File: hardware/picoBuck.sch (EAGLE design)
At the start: 29 parts

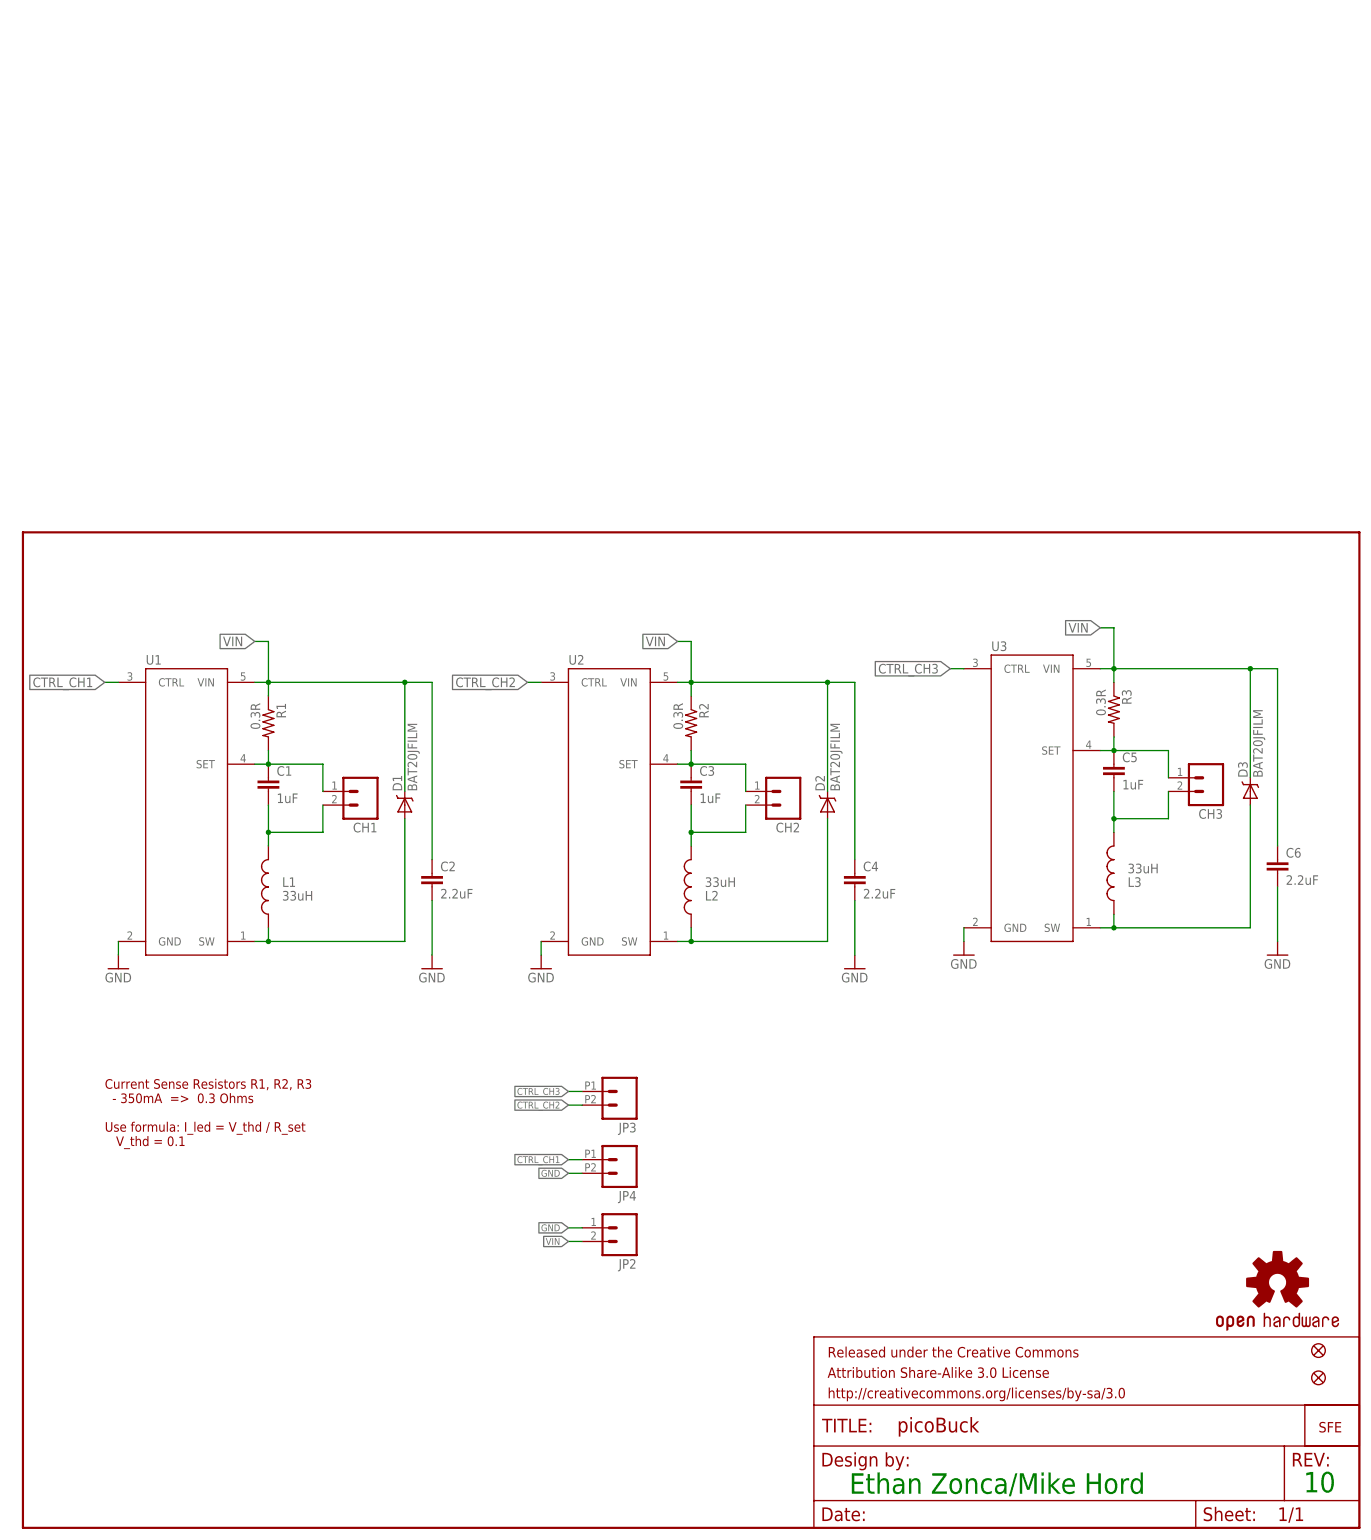
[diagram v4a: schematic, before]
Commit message: High power initial revision - added 2nd sense resistor and solder jumper - changed diode to higher voltage version - changed input cap to higher voltage version
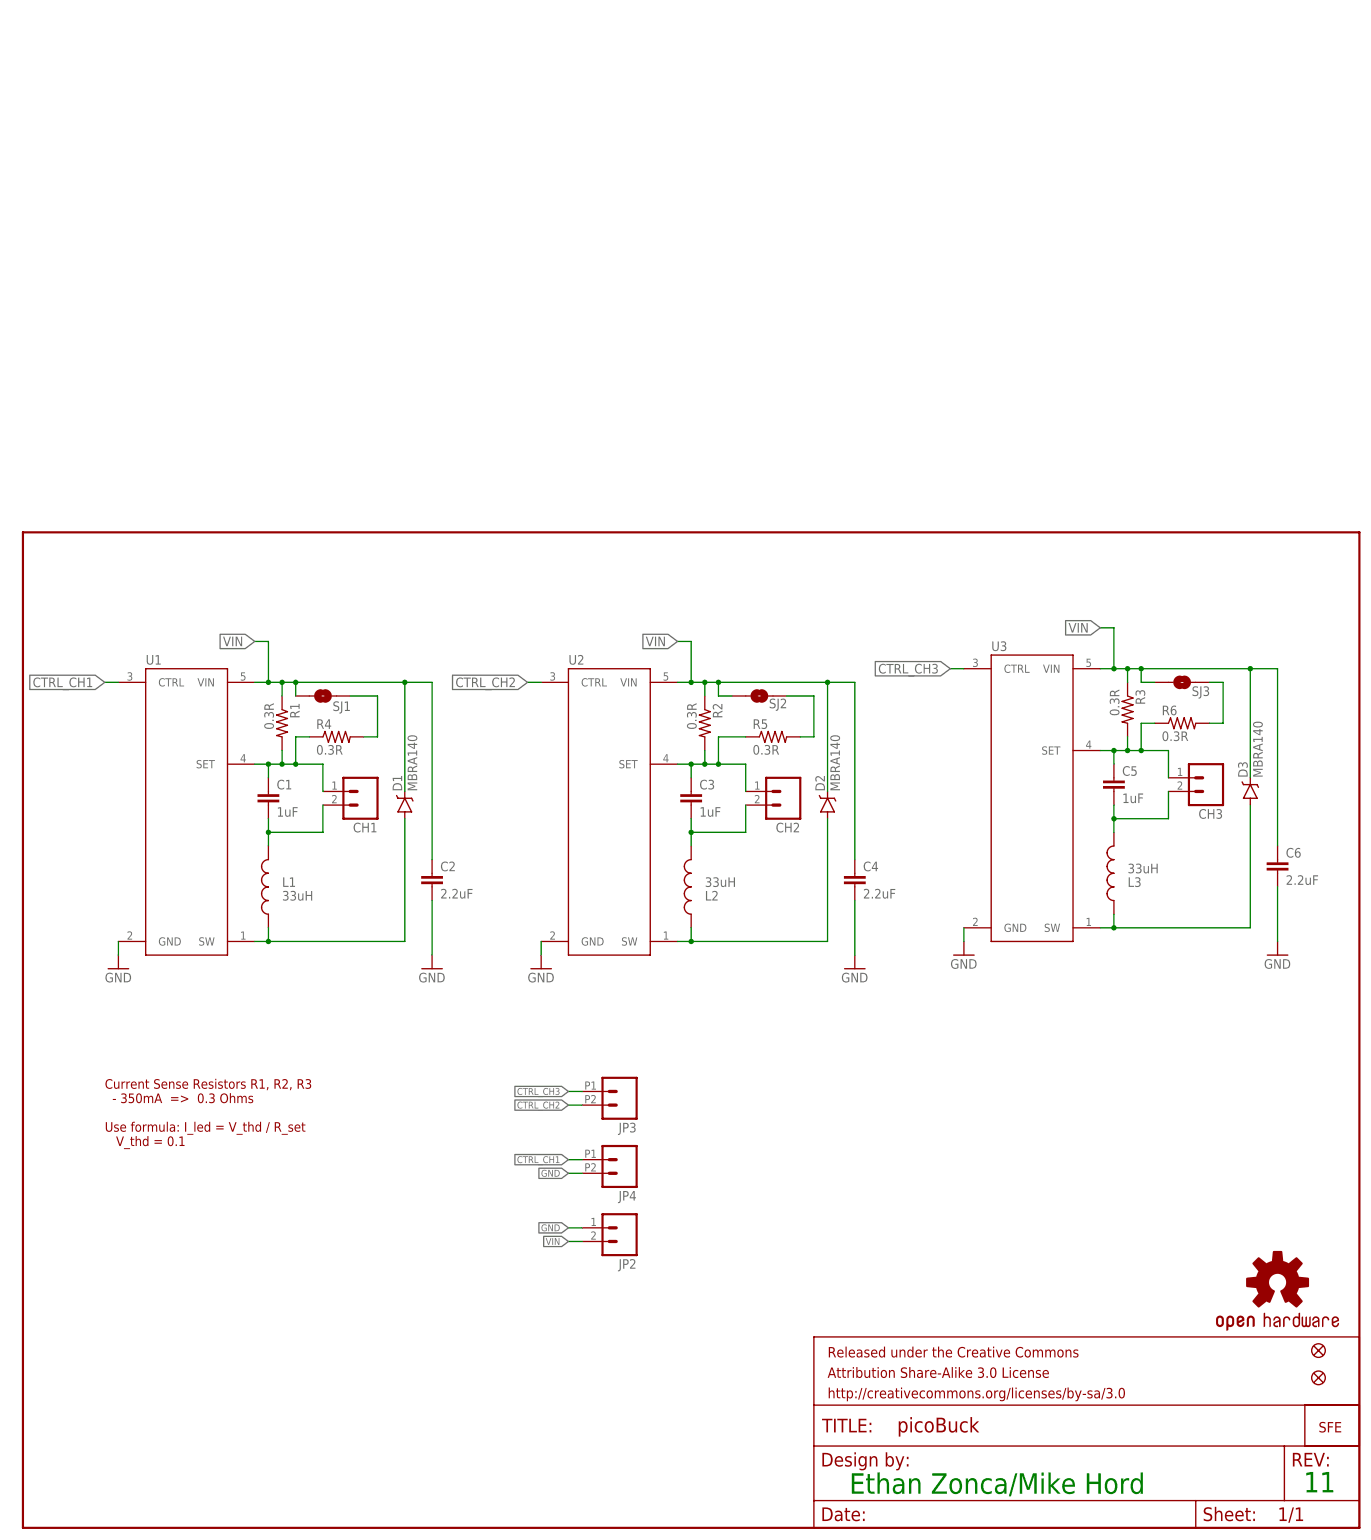
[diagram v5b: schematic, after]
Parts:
- added R4, R5, R6: 0.3R, SparkFun-Resistors:0.3OHM-1/8W-1%(0805)
- added SJ1, SJ2, SJ3: JUMPER-PAD-2-NO, SparkFun-Passives:JUMPER-PAD-2-NO
- D1, D2, D3: value BAT20JFILM -> MBRA140; device SparkFun-DiscreteSemi:BAT20JFILM -> SparkFun-DiscreteSemi:DIODE-SCHOTTKY-MBRA140
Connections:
- removed net N$18: C5.1, CH3.1, R3.2, U3.SET
- new net N$1: C5.1, CH3.1, R3.2, R6.1, U3.SET
- new net N$2: R4.2, SJ1.2
- new net N$3: R5.2, SJ2.2
- new net N$7: R6.2, SJ3.2
- net N$11: now also R4.1
- net N$13: now also R5.1
- net VIN: now also SJ1.1, SJ2.1, SJ3.1
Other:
- note added: "11"
- note removed: "10"
- moved on the sheet: C1, C3, C5, R1, R2, R3

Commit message: Make files as they were before I started monkeying with them
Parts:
- added STANDOFF1, STANDOFF2: STAND-OFF, SparkFun-Electromechanical:STAND-OFF
- U1, U2, U3: value (none) -> AL8805
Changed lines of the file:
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@@
 </classes>
 <parts>
-<part name="U2" library="SparkFun-PowerIC" deviceset="AL8805" device=""/>
+<part name="U2" library="SparkFun-PowerIC" deviceset="AL8805" device="" value="AL8805"/>
 <part name="R2" library="SparkFun-Resistors" deviceset="0.3OHM-1/8W-1%(0805)" device="" value="0.3R"/>
 <part name="C3" library="SparkFun-Capacitors" deviceset="1.0UF-25V-+80/-20(0805)" device="" value="1uF"/>
@@
 <part name="GND12" library="SparkFun" deviceset="GND" device=""/>
 <part name="GND1" library="SparkFun" deviceset="GND" device=""/>
-<part name="U1" library="SparkFun-PowerIC" deviceset="AL8805" device=""/>
+<part name="U1" library="SparkFun-PowerIC" deviceset="AL8805" device="" value="AL8805"/>
 <part name="R1" library="SparkFun-Resistors" deviceset="0.3OHM-1/8W-1%(0805)" device="" value="0.3R"/>
 <part name="C1" library="SparkFun-Capacitors" deviceset="1.0UF-25V-+80/-20(0805)" device="" value="1uF"/>
@@
 <part name="GND6" library="SparkFun" deviceset="GND" device=""/>
 <part name="GND13" library="SparkFun" deviceset="GND" device=""/>
-<part name="U3" library="SparkFun-PowerIC" deviceset="AL8805" device=""/>
+<part name="U3" library="SparkFun-PowerIC" deviceset="AL8805" device="" value="AL8805"/>
 <part name="R3" library="SparkFun-Resistors" deviceset="0.3OHM-1/8W-1%(0805)" device="" value="0.3R"/>
 <part name="C6" library="SparkFun-Capacitors" deviceset="2.2UF-25V-+80/-20(0805)" device="" value="2.2uF"/>
@@
 <part name="R5" library="SparkFun-Resistors" deviceset="0.3OHM-1/8W-1%(0805)" device="" value="0.3R"/>
 <part name="R6" library="SparkFun-Resistors" deviceset="0.3OHM-1/8W-1%(0805)" device="" value="0.3R"/>
+<part name="STANDOFF1" library="SparkFun-Electromechanical" deviceset="STAND-OFF" device=""/>
+<part name="STANDOFF2" library="SparkFun-Electromechanical" deviceset="STAND-OFF" device=""/>
 </parts>
 <sheets>
@@
 <instance part="LOGO2" gate="G$1" x="241.3" y="17.78"/>
 <instance part="FRAME1" gate="G$1" x="0" y="0"/>
-<instance part="FRAME1" gate="G$2" x="147.32" y="0"/>
+<instance part="FRAME1" gate="V" x="147.32" y="0"/>
 <instance part="JP3" gate="G$1" x="111.76" y="81.28" smashed="yes" rot="R180">
 <attribute name="NAME" x="114.3" y="75.438" size="1.778" layer="95" rot="R180"/>
@@
 <instance part="R5" gate="G$1" x="139.7" y="147.32"/>
 <instance part="R6" gate="G$1" x="215.9" y="149.86"/>
+<instance part="STANDOFF1" gate="G$1" x="236.22" y="27.94"/>
+<instance part="STANDOFF2" gate="G$1" x="236.22" y="33.02"/>
 </instances>
 <busses>

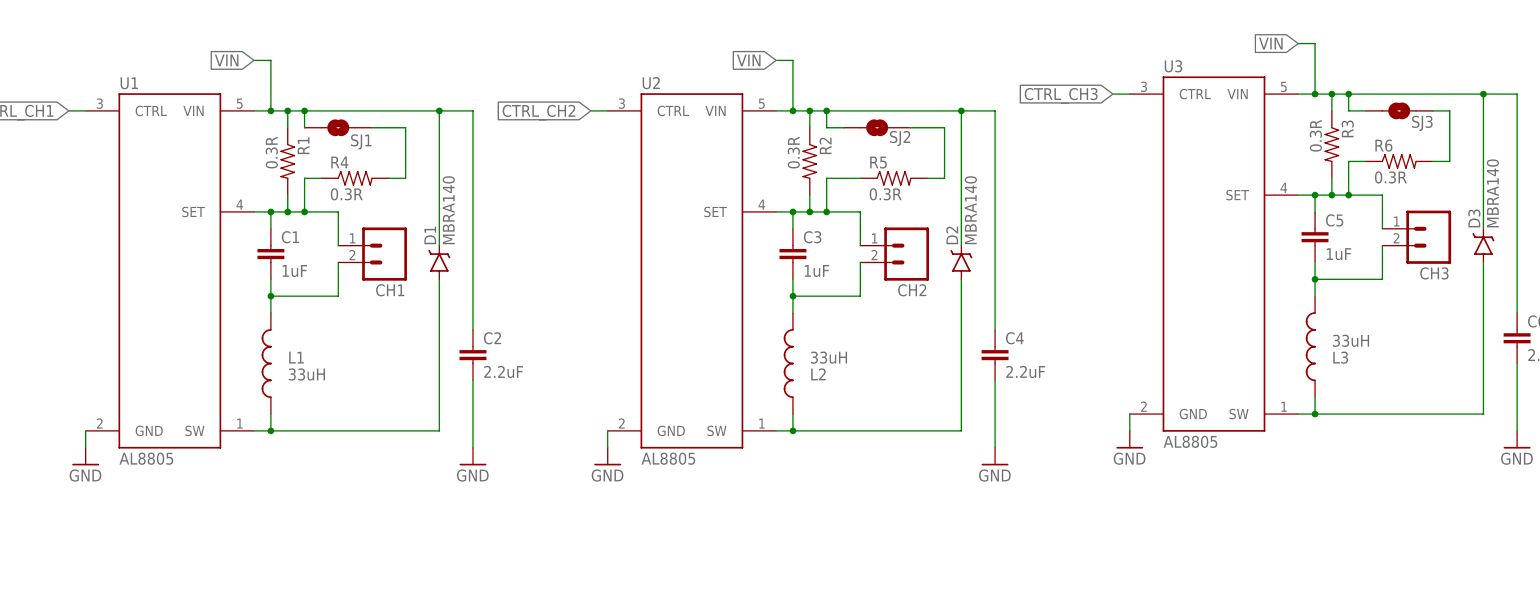
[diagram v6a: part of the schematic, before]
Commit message: Updated library for some silk changes
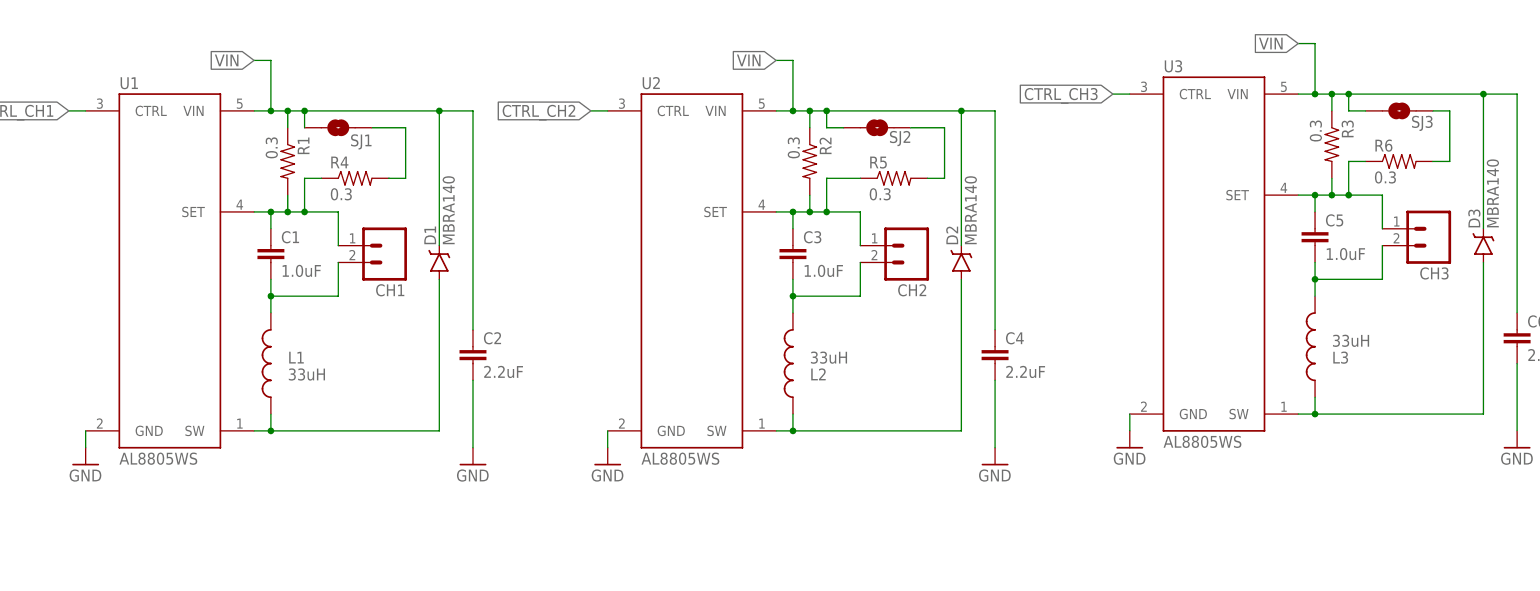
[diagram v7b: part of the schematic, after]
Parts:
- C1, C3, C5: value 1uF -> 1.0uF; device SparkFun-Capacitors:1.0UF-25V-+80/-20(0805) -> SparkFun-Capacitors:1.0UF-25V-+80/-20(0805)"
- R1, R2, R3, R4, R5, R6: value 0.3R -> 0.3
- U1, U2, U3: value AL8805 -> AL8805WS
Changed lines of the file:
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@@
 </classes>
 <parts>
-<part name="U2" library="SparkFun-PowerIC" deviceset="AL8805" device="" value="AL8805"/>
-<part name="R2" library="SparkFun-Resistors" deviceset="0.3OHM-1/8W-1%(0805)" device="" value="0.3R"/>
-<part name="C3" library="SparkFun-Capacitors" deviceset="1.0UF-25V-+80/-20(0805)" device="" value="1uF"/>
+<part name="U2" library="SparkFun-PowerIC" deviceset="AL8805" device="" value="AL8805WS"/>
+<part name="R2" library="SparkFun-Resistors" deviceset="0.3OHM-1/8W-1%(0805)" device="" value="0.3"/>
+<part name="C3" library="SparkFun-Capacitors" deviceset="1.0UF-25V-+80/-20(0805)" device="&quot;" value="1.0uF"/>
 <part name="C4" library="SparkFun-Capacitors" deviceset="2.2UF-25V-+80/-20(0805)" device="" value="2.2uF"/>
 <part name="GND12" library="SparkFun" deviceset="GND" device=""/>
 <part name="GND1" library="SparkFun" deviceset="GND" device=""/>
-<part name="U1" library="SparkFun-PowerIC" deviceset="AL8805" device="" value="AL8805"/>
-<part name="R1" library="SparkFun-Resistors" deviceset="0.3OHM-1/8W-1%(0805)" device="" value="0.3R"/>
-<part name="C1" library="SparkFun-Capacitors" deviceset="1.0UF-25V-+80/-20(0805)" device="" value="1uF"/>
+<part name="U1" library="SparkFun-PowerIC" deviceset="AL8805" device="" value="AL8805WS"/>
+<part name="R1" library="SparkFun-Resistors" deviceset="0.3OHM-1/8W-1%(0805)" device="" value="0.3"/>
+<part name="C1" library="SparkFun-Capacitors" deviceset="1.0UF-25V-+80/-20(0805)" device="&quot;" value="1.0uF"/>
 <part name="C2" library="SparkFun-Capacitors" deviceset="2.2UF-25V-+80/-20(0805)" device="" value="2.2uF"/>
 <part name="GND6" library="SparkFun" deviceset="GND" device=""/>
 <part name="GND13" library="SparkFun" deviceset="GND" device=""/>
-<part name="U3" library="SparkFun-PowerIC" deviceset="AL8805" device="" value="AL8805"/>
-<part name="R3" library="SparkFun-Resistors" deviceset="0.3OHM-1/8W-1%(0805)" device="" value="0.3R"/>
+<part name="U3" library="SparkFun-PowerIC" deviceset="AL8805" device="" value="AL8805WS"/>
+<part name="R3" library="SparkFun-Resistors" deviceset="0.3OHM-1/8W-1%(0805)" device="" value="0.3"/>
 <part name="C6" library="SparkFun-Capacitors" deviceset="2.2UF-25V-+80/-20(0805)" device="" value="2.2uF"/>
 <part name="GND14" library="SparkFun" deviceset="GND" device=""/>
@@
 <part name="CH1" library="SparkFun" deviceset="M02" device="3.5MM_LOCK"/>
 <part name="CH3" library="SparkFun" deviceset="M02" device="3.5MM_LOCK"/>
-<part name="C5" library="SparkFun-Capacitors" deviceset="1.0UF-25V-+80/-20(0805)" device="" value="1uF"/>
+<part name="C5" library="SparkFun-Capacitors" deviceset="1.0UF-25V-+80/-20(0805)" device="&quot;" value="1.0uF"/>
 <part name="D1" library="SparkFun-DiscreteSemi" deviceset="DIODE-SCHOTTKY" device="-MBRA140" value="MBRA140"/>
 <part name="D2" library="SparkFun-DiscreteSemi" deviceset="DIODE-SCHOTTKY" device="-MBRA140" value="MBRA140"/>
@@
 <part name="SJ2" library="SparkFun-Passives" deviceset="JUMPER-PAD-2-NO" device=""/>
 <part name="SJ3" library="SparkFun-Passives" deviceset="JUMPER-PAD-2-NO" device=""/>
-<part name="R4" library="SparkFun-Resistors" deviceset="0.3OHM-1/8W-1%(0805)" device="" value="0.3R"/>
-<part name="R5" library="SparkFun-Resistors" deviceset="0.3OHM-1/8W-1%(0805)" device="" value="0.3R"/>
-<part name="R6" library="SparkFun-Resistors" deviceset="0.3OHM-1/8W-1%(0805)" device="" value="0.3R"/>
+<part name="R4" library="SparkFun-Resistors" deviceset="0.3OHM-1/8W-1%(0805)" device="" value="0.3"/>
+<part name="R5" library="SparkFun-Resistors" deviceset="0.3OHM-1/8W-1%(0805)" device="" value="0.3"/>
+<part name="R6" library="SparkFun-Resistors" deviceset="0.3OHM-1/8W-1%(0805)" device="" value="0.3"/>
 <part name="STANDOFF1" library="SparkFun-Electromechanical" deviceset="STAND-OFF" device=""/>
 <part name="STANDOFF2" library="SparkFun-Electromechanical" deviceset="STAND-OFF" device=""/>

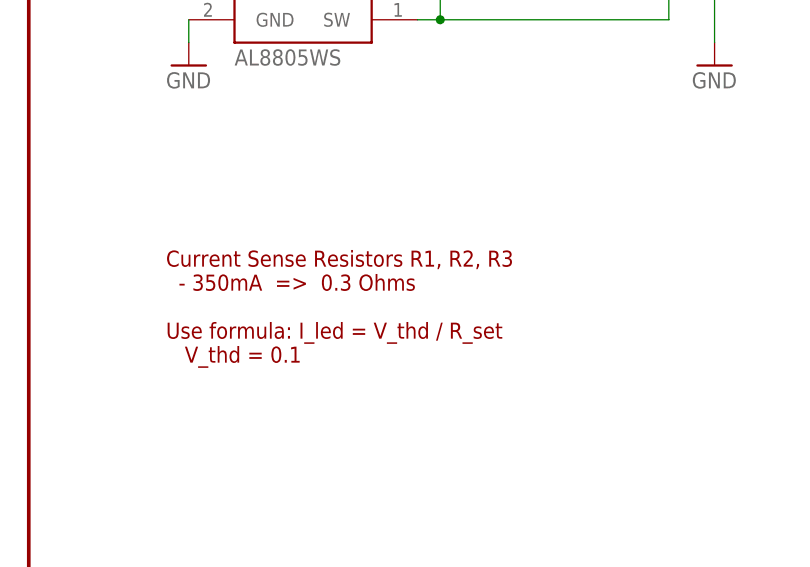
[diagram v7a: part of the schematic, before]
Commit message: Add vin range to sch
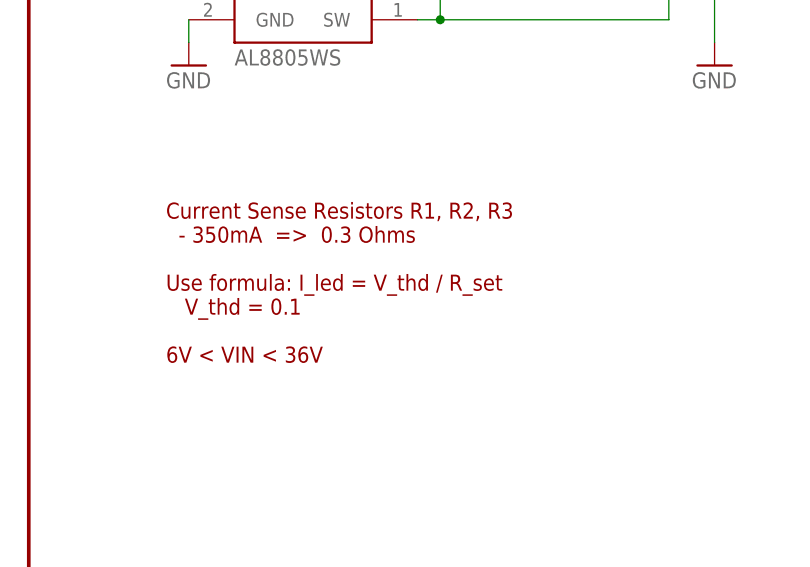
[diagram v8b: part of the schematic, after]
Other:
- note added: "Current Sense Resistors R1, R2, R3 - 350mA => 0.3 Ohms Use formula: I_led = V_thd / R_set V_thd = 0.1 6V < VIN < 36V"
- note removed: "Current Sense Resistors R1, R2, R3 - 350mA => 0.3 Ohms Use formula: I_led = V_thd / R_set V_thd = 0.1"
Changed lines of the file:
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@@
 Use formula: I_led = V_thd / R_set
    V_thd = 0.1
-</text>
+6V &lt; VIN &lt; 36V</text>
 <text x="238.506" y="6.604" size="3.81" layer="91">11</text>
 <text x="153.924" y="6.35" size="3.81" layer="91">Ethan Zonca/Mike Hord</text>
